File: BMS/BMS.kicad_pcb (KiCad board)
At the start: 2 copper layers, 30 x 25 mm, 24 parts, among them IC1 DW01A, J1 Conn_01x02, J2 Conn_01x02, J3 Conn_01x02, P1 USB_C_Plug_USB2.0, Q1 AO3401A, Q2 FS8205A, U1 TP4056

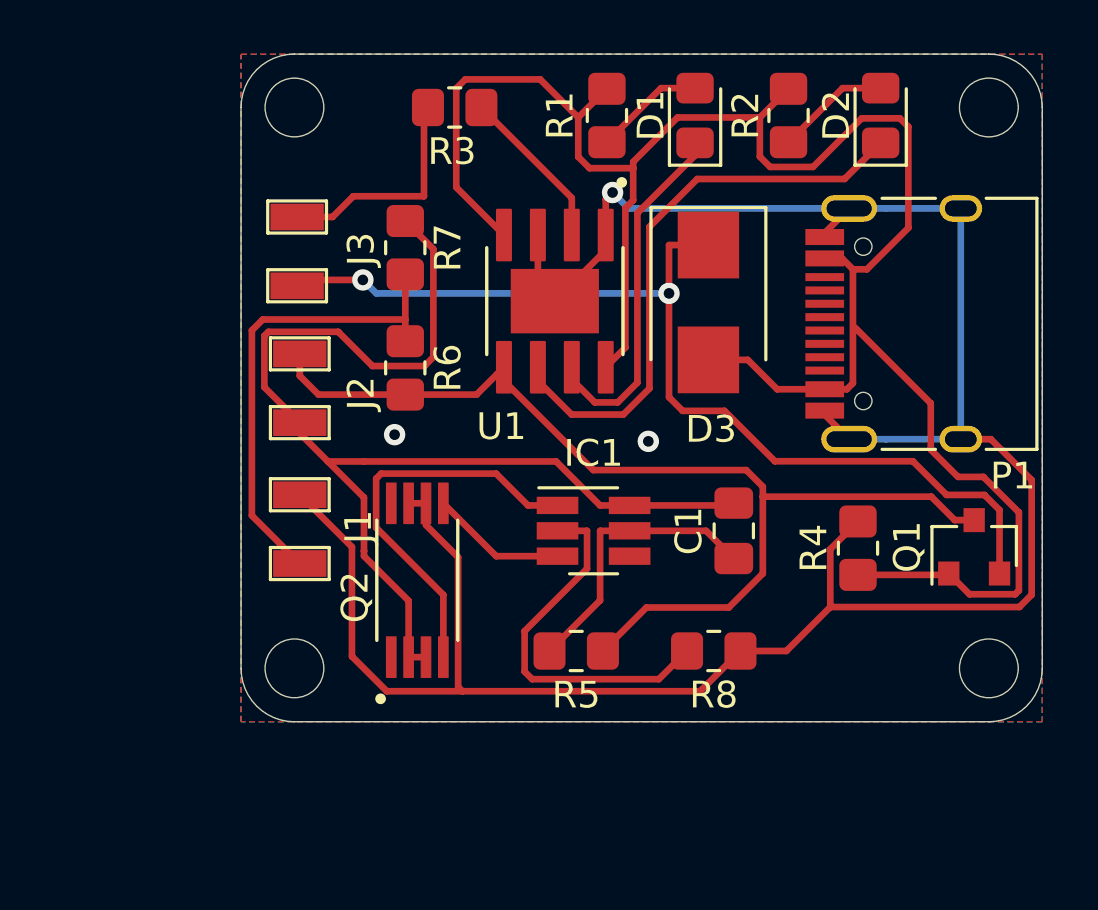
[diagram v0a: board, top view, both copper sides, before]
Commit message: PCB: USB C receptacle moved close to PCB edge
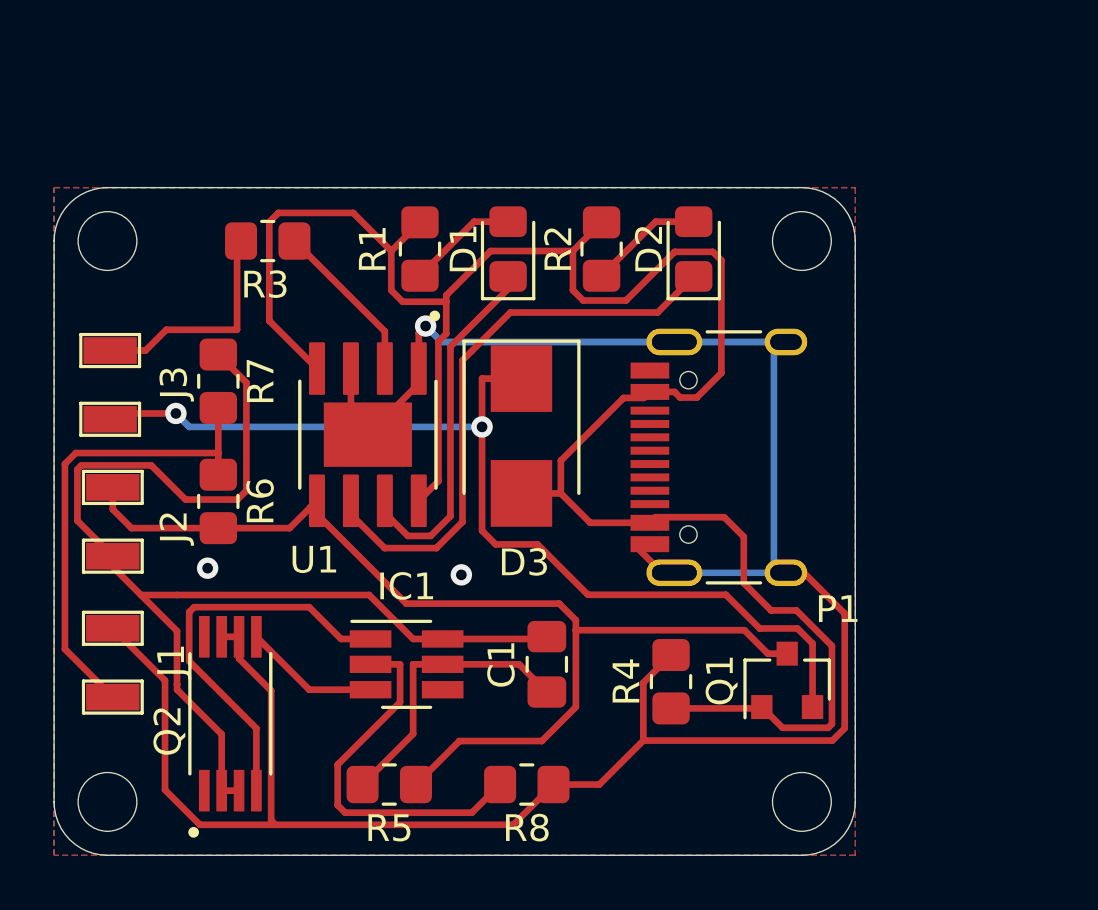
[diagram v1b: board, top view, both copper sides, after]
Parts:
- P1: footprint Connector_USB:USB_C_Receptacle_HRO_TYPE-C-31-M-12 -> Board:USB_C_Receptacle_HRO_TYPE-C-31-M-12
- moved C1 8.60 mm to (150.4, 99.8)
- moved D1 8.60 mm to (149.0, 84.3)
- moved D2 8.60 mm to (155.9, 84.3)
- moved D3 8.60 mm to (149.5, 91.3)
- moved H1 8.60 mm to (134.0, 84.0)
- moved H2 8.60 mm to (160.0, 84.0)
- moved H3 8.60 mm to (160.0, 105.0)
- moved H4 8.60 mm to (134.0, 105.0)
- moved IC1 8.60 mm to (145.2, 99.8)
- moved J1 8.60 mm to (131.1, 99.6)
- moved J2 8.60 mm to (137.3, 94.7)
- moved J3 8.60 mm to (131.0, 89.2)
- moved Q1 8.60 mm to (159.4, 100.5)
- moved Q2 8.60 mm to (138.6, 101.7)
- moved R1 8.60 mm to (145.7, 84.3)
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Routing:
- net GND: track 100.0 -> 98.7 mm
- net /VBUS: track 77.2 -> 78.4 mm
